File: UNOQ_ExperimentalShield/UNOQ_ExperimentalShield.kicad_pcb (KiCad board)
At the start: 4 copper layers, 68.6 x 53.3 mm, 124 parts, among them CN1 485, CN2 USB, CN3 Can, CN4 Can, CN5 485, J1 Power, J2 Digital/PWM, J3 Analog, J4 Digital/PWM, SW1 Usr1, SW2 Usr1, U1 25LCxxx, U2 TMP102xxDRL, U3 MAX3485ESA-MS, U4 CH340N, U5 TJA1051T-3, U7 ATECC608A-SSHDA

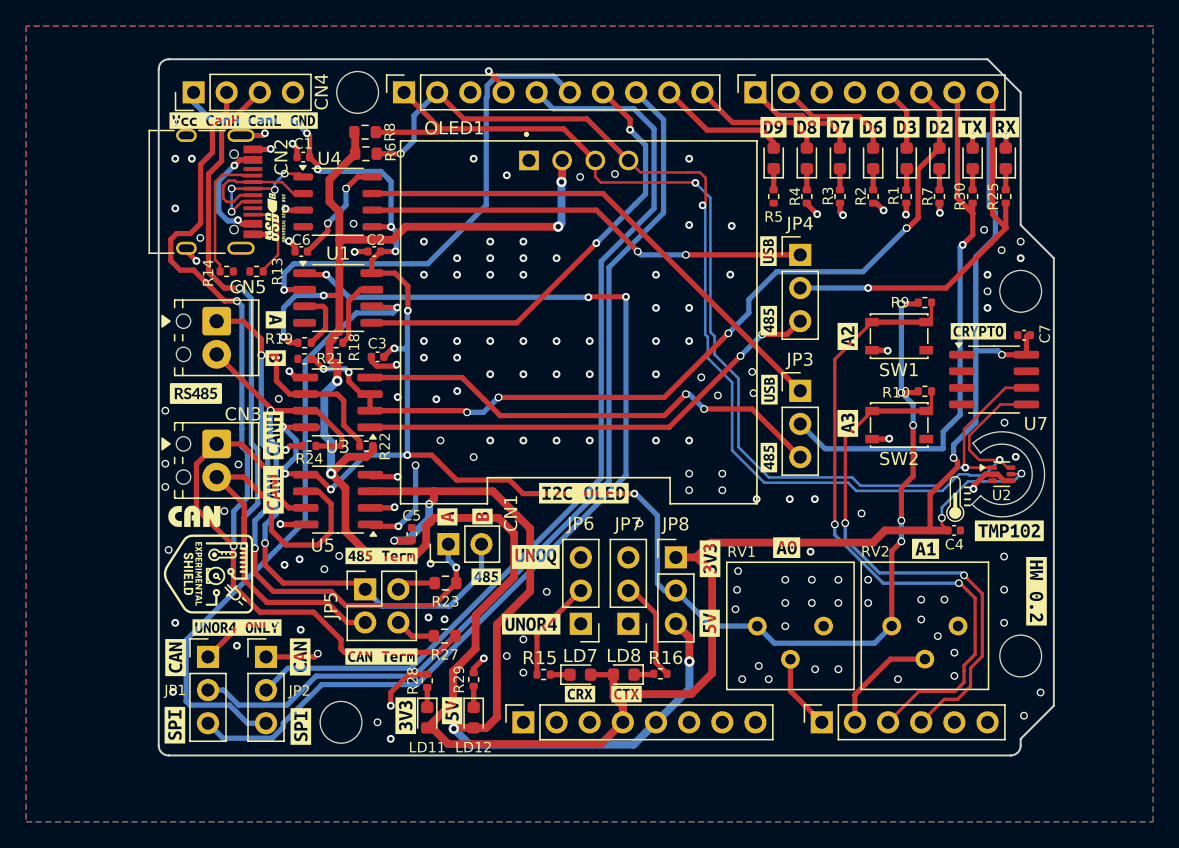
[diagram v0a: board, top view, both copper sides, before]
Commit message: Added unoq (without can) test sketch
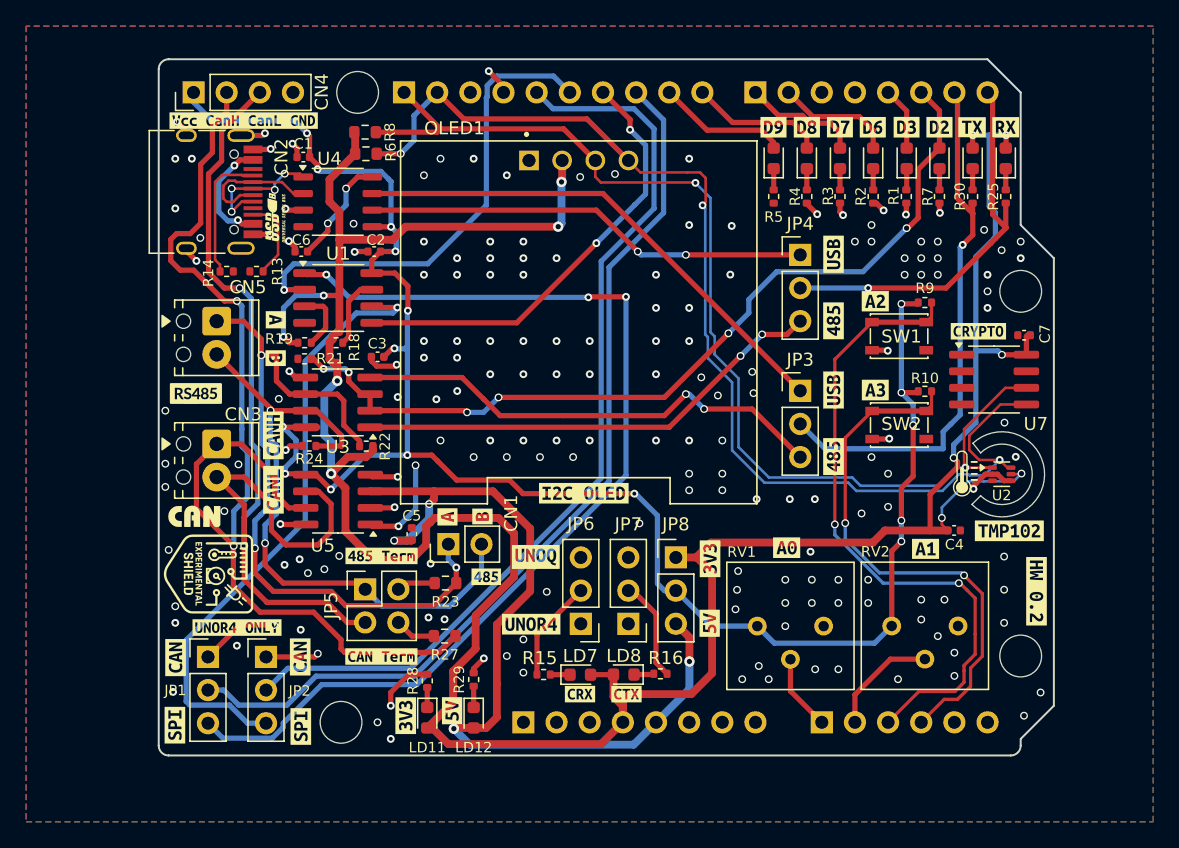
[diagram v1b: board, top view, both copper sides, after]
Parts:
- removed kibuzzard-695F8C20: G***, kibuzzard-695F8C20
- removed kibuzzard-695F8C29: G***, kibuzzard-695F8C29
- removed kibuzzard-695F8C32: G***, kibuzzard-695F8C32
- removed kibuzzard-695F8C3A: G***, kibuzzard-695F8C3A
- added kibuzzard-69ECB574: G***, kibuzzard-69ECB574, F.Cu at (151.7, 72.0)
- added kibuzzard-69ECB57B: G***, kibuzzard-69ECB57B, F.Cu at (151.7, 77.1)
- added kibuzzard-69ECB59B: G***, kibuzzard-69ECB59B, F.Cu at (151.7, 66.7)
- added kibuzzard-69ECB5A8: G***, kibuzzard-69ECB5A8, F.Cu at (151.7, 61.6)
- J1, J2, J3, J4: moved to B.Cu
- R1, R2, R3, R4, R5, R7: value 1k -> 1.5k
- moved kibuzzard-69E2216E 3.43 mm to (154.9, 65.2), turned to 0 degrees
- moved kibuzzard-69E22173 3.31 mm to (154.9, 72.0), turned to 0 degrees
- moved G*** 2.02 mm to (161.8, 78.4)
- turned J1 to -90 degrees
- turned J2 to -90 degrees
- turned J3 to -90 degrees
- turned J4 to -90 degrees
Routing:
- net GND: vias 152 -> 174
